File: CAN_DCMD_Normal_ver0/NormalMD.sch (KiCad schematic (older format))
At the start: 224 parts, among them P1 SWD, P10 OUT_1, P11 ENC_0, P13 ENC_1, P14 I/O_1, P15 OUT_0, P2 VALVE, P3 CAN, P4 CAN, P5 SERIAL, P6 I/O_0, P7 FAN, P8 BATT_IN, P9 BATT_IN, Q1 MOSFET_N, Q10 NPN, Q2 MOSFET_N, Q3 MOSFET_N, Q4 MOSFET_N, Q5 MOSFET_N, Q6 MOSFET_N, Q7 MOSFET_N, Q8 MOSFET_N, Q9 NPN, SW1 RST, SW3 SW0, SW4 SW1, U1 MAX3051, U11 POWER_ON, U12 SI8274, U14 SI8274, U15 AZ1086H, U16 LOGO, U17 AQM0802, U19 ADRESS, U2 BD9G101, U3 STM32F405RG, U4 SI8274, U5 SI8900, U6 ADC_~RST, U7 BD9G101G, U8 SI8274, U9 BD33FA1, Y1 8MHz

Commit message: 配置しただけで分かるやばいやつ
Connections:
- net VALVE0: now also U3.50 (TIM2_CH1_ETR/PA15)
- net VALVE1: now also U3.51 (PC10/UART4_TX/USART3_TX)
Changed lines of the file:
@@
 	1    0    0    -1
 $EndComp
+Text Label 4550 7125 2    50   ~ 0
+VALVE1
+Text Label 8950 5925 0    50   ~ 0
+VALVE0
 $EndSCHEMATC

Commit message: 電流制御MD(仮)配線(仮)完成(仮)
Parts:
- R37: value 50k -> 3.9k
- R38: value 10k -> 680
- R57, R60, R75, R76: value 2m -> 1m
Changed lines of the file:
@@
 P 5200 1800
 F 0 "R37" H 5270 1846 50  0000 L CNN
-F 1 "50k" H 5270 1755 50  0000 L CNN
+F 1 "3.9k" H 5270 1755 50  0000 L CNN
 F 2 "Resistor_SMD:R_0603_1608Metric" V 5130 1800 50  0001 C CNN
 F 3 "~" H 5200 1800 50  0001 C CNN
@@
 P 5200 2150
 F 0 "R38" H 5270 2196 50  0000 L CNN
-F 1 "10k" H 5270 2105 50  0000 L CNN
+F 1 "680" H 5270 2105 50  0000 L CNN
 F 2 "Resistor_SMD:R_0603_1608Metric" V 5130 2150 50  0001 C CNN
 F 3 "~" H 5200 2150 50  0001 C CNN
@@
 P 18650 6250
 F 0 "R57" V 18443 6250 50  0000 C CNN
-F 1 "2m" V 18534 6250 50  0000 C CNN
+F 1 "1m" V 18534 6250 50  0000 C CNN
 F 2 "Mizz_lib:R_2010_5025Metric" V 18580 6250 50  0001 C CNN
 F 3 "~" H 18650 6250 50  0001 C CNN
@@
 P 18650 6550
 F 0 "R60" V 18443 6550 50  0000 C CNN
-F 1 "2m" V 18534 6550 50  0000 C CNN
+F 1 "1m" V 18534 6550 50  0000 C CNN
 F 2 "Mizz_lib:R_2010_5025Metric" V 18580 6550 50  0001 C CNN
 F 3 "~" H 18650 6550 50  0001 C CNN
@@
 P 18650 9950
 F 0 "R75" V 18443 9950 50  0000 C CNN
-F 1 "2m" V 18534 9950 50  0000 C CNN
+F 1 "1m" V 18534 9950 50  0000 C CNN
 F 2 "Mizz_lib:R_2010_5025Metric" V 18580 9950 50  0001 C CNN
 F 3 "~" H 18650 9950 50  0001 C CNN
@@
 P 18650 10250
 F 0 "R76" V 18443 10250 50  0000 C CNN
-F 1 "2m" V 18534 10250 50  0000 C CNN
+F 1 "1m" V 18534 10250 50  0000 C CNN
 F 2 "Mizz_lib:R_2010_5025Metric" V 18580 10250 50  0001 C CNN
 F 3 "~" H 18650 10250 50  0001 C CNN

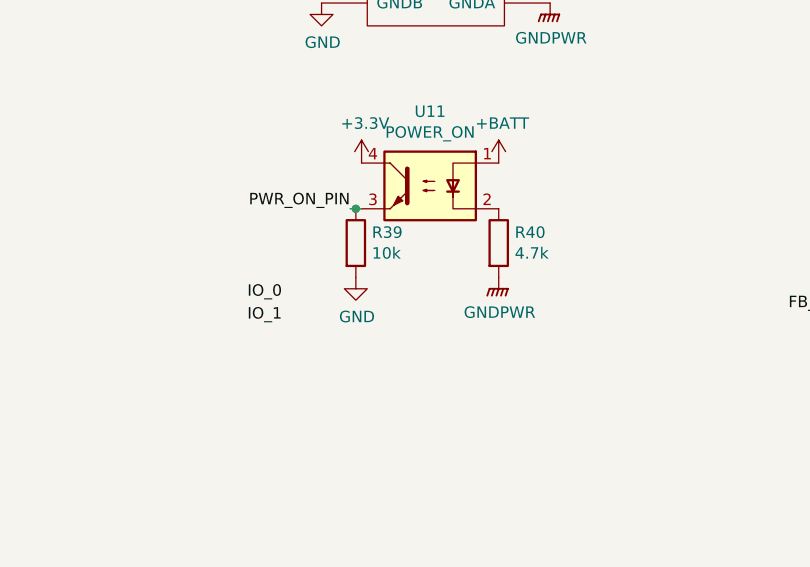
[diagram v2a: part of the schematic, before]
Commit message: 抵抗値を実装されているものに変更した
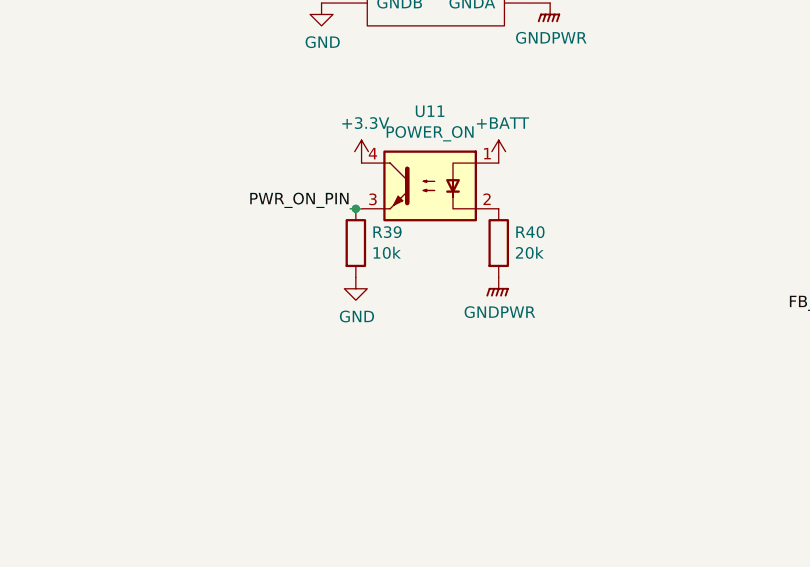
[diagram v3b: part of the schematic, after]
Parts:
- R40: value 4.7k -> 20k
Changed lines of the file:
@@
 EESchema Schematic File Version 4
-LIBS:NormalMD-cache
 EELAYER 30 0
 EELAYER END
@@
 Text Label 7800 13375 2    50   ~ 0
 USART2_RX
-Text Label 13950 4625 0    50   ~ 0
-IO_0
 $Comp
 L NormalMD-rescue:R-Device-MD_Enbarr_x2-rescue-F4_CAN_DCMD-rescue-SteerMD-rescue R4
@@
 P 15050 4375
 F 0 "R40" H 15120 4421 50  0000 L CNN
-F 1 "4.7k" H 15120 4330 50  0000 L CNN
+F 1 "20k" H 15120 4330 50  0000 L CNN
 F 2 "Resistor_SMD:R_0603_1608Metric" V 14980 4375 50  0001 C CNN
 F 3 "~" H 15050 4375 50  0001 C CNN
@@
 Text Label 8950 5225 0    50   ~ 0
 SW0
-Text Label 13950 4725 0    50   ~ 0
-IO_1
 Text Label 19200 2075 2    50   ~ 0
 OUT0_L

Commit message: 上げ忘れていた工大祭モータドライバ(前身開発基板)とJetsonNanoの電源基板関係
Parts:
- AMP1, AMP2: symbol Miz:TSC103 -> NormalMD-rescue:TSC103-Miz-NormalMD-rescue
- Q1, Q2, Q3, Q4, Q5, Q6, Q7, Q8: symbol NormalMD-rescue:MOSFET_N-Miz-F4_CAN_DCMD-rescue-SteerMD-rescue -> NormalMD-rescue:MOSFET_N-Miz-F4_CAN_DCMD-rescue-SteerMD-rescue-NormalMD-rescue
- U12, U14, U4, U8: symbol NormalMD-rescue:SI8274-Miz-F4_CAN_DCMD-rescue-SteerMD-rescue -> NormalMD-rescue:SI8274-Miz-F4_CAN_DCMD-rescue-SteerMD-rescue-NormalMD-rescue
- U16: symbol NormalMD-rescue:LOGO-myDevice-MD_Enbarr_x2-rescue-F4_CAN_DCMD-rescue-SteerMD-rescue -> NormalMD-rescue:LOGO-myDevice-MD_Enbarr_x2-rescue-F4_CAN_DCMD-rescue-SteerMD-rescue-NormalMD-rescue
- U2: symbol Miz:AP3211 -> NormalMD-rescue:AP3211-Miz
- U3: symbol NormalMD-rescue:STM32F405RG_excerpt-stm32f405rg_excerpt-Miz-MD_Enbarr_x2-rescue-F4_CAN_DCMD-rescue-SteerMD-rescue -> NormalMD-rescue:STM32F405RG_excerpt-stm32f405rg_excerpt-Miz-MD_Enbarr_x2-rescue-F4_CAN_DCMD-rescue-SteerMD-rescue-Norma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
- U5: symbol NormalMD-rescue:SI8900-Hori_lib-MD_Enbarr_x2-rescue-F4_CAN_DCMD-rescue-SteerMD-rescue -> NormalMD-rescue:SI8900-Hori_lib-MD_Enbarr_x2-rescue-F4_CAN_DCMD-rescue-SteerMD-rescue-NormalMD-rescue
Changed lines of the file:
@@
 EESchema Schematic File Version 4
+LIBS:NormalMD-cache
 EELAYER 30 0
 EELAYER END
@@
 $EndDescr
 $Comp
-L NormalMD-rescue:STM32F405RG_excerpt-stm32f405rg_excerpt-Miz-MD_Enbarr_x2-rescue-F4_CAN_DCMD-rescue-SteerMD-rescue U3
+L NormalMD-rescue:STM32F405RG_excerpt-stm32f405rg_excerpt-Miz-MD_Enbarr_x2-rescue-F4_CAN_DCMD-rescue-SteerMD-rescue-NormalMD-rescue U3
 U 1 1 5E0DD671
 P 6750 6025
@@
 $EndComp
 $Comp
-L NormalMD-rescue:SI8900-Hori_lib-MD_Enbarr_x2-rescue-F4_CAN_DCMD-rescue-SteerMD-rescue U5
+L NormalMD-rescue:SI8900-Hori_lib-MD_Enbarr_x2-rescue-F4_CAN_DCMD-rescue-SteerMD-rescue-NormalMD-rescue U5
 U 1 1 5E1CE2F1
 P 14775 2975
@@
 	18825 3000 18700 3000
 $Comp
-L Miz:AP3211 U2
+L NormalMD-rescue:AP3211-Miz U2
 U 1 1 5E588240
 P 4175 1850
@@
 Current0
 $Comp
-L NormalMD-rescue:LOGO-myDevice-MD_Enbarr_x2-rescue-F4_CAN_DCMD-rescue-SteerMD-rescue U16
+L NormalMD-rescue:LOGO-myDevice-MD_Enbarr_x2-rescue-F4_CAN_DCMD-rescue-SteerMD-rescue-NormalMD-rescue U16
 U 1 1 5D9F257F
 P 21750 2850
@@
 Connection ~ 10550 9875
 $Comp
-L Miz:LOGO_Monster #G1
+L NormalMD-rescue:LOGO_Monster-Miz #G1
 U 1 1 5E034095
 P 21725 2025
@@
 	18650 7650 18650 7725
 $Comp
-L Miz:TSC103 AMP2
+L NormalMD-rescue:TSC103-Miz-NormalMD-rescue AMP2
 U 1 1 5E2A539A
 P 18650 10875
@@
 	18100 12575 18650 12575
 $Comp
-L Miz:TSC103 AMP1
+L NormalMD-rescue:TSC103-Miz-NormalMD-rescue AMP1
 U 1 1 5E1F1A95
 P 18650 7175
@@
 $EndComp
 $Comp
-L NormalMD-rescue:SI8274-Miz-F4_CAN_DCMD-rescue-SteerMD-rescue U4
+L NormalMD-rescue:SI8274-Miz-F4_CAN_DCMD-rescue-SteerMD-rescue-NormalMD-rescue U4
 U 1 1 5DD10035
 P 16500 8325
@@
 $EndComp
 $Comp
-L NormalMD-rescue:MOSFET_N-Miz-F4_CAN_DCMD-rescue-SteerMD-rescue Q2
+L NormalMD-rescue:MOSFET_N-Miz-F4_CAN_DCMD-rescue-SteerMD-rescue-NormalMD-rescue Q2
 U 1 1 5DD192A7
 P 18000 8675
@@
 	17125 8825 17800 8825
 $Comp
-L NormalMD-rescue:MOSFET_N-Miz-F4_CAN_DCMD-rescue-SteerMD-rescue Q1
+L NormalMD-rescue:MOSFET_N-Miz-F4_CAN_DCMD-rescue-SteerMD-rescue-NormalMD-rescue Q1
 U 1 1 5DF47111
 P 18000 7925
@@
 	17650 7925 17800 7925
 $Comp
-L NormalMD-rescue:MOSFET_N-Miz-F4_CAN_DCMD-rescue-SteerMD-rescue Q5
+L NormalMD-rescue:MOSFET_N-Miz-F4_CAN_DCMD-rescue-SteerMD-rescue-NormalMD-rescue Q5
 U 1 1 5DF92975
 P 19300 7925
@@
 $EndComp
 $Comp
-L NormalMD-rescue:MOSFET_N-Miz-F4_CAN_DCMD-rescue-SteerMD-rescue Q6
+L NormalMD-rescue:MOSFET_N-Miz-F4_CAN_DCMD-rescue-SteerMD-rescue-NormalMD-rescue Q6
 U 1 1 5DF933DA
 P 19300 8675
@@
 Connection ~ 18100 8875
 $Comp
-L NormalMD-rescue:SI8274-Miz-F4_CAN_DCMD-rescue-SteerMD-rescue U12
+L NormalMD-rescue:SI8274-Miz-F4_CAN_DCMD-rescue-SteerMD-rescue-NormalMD-rescue U12
 U 1 1 5DFB7F6D
 P 20800 8325
@@
 $EndComp
 $Comp
-L NormalMD-rescue:SI8274-Miz-F4_CAN_DCMD-rescue-SteerMD-rescue U8
+L NormalMD-rescue:SI8274-Miz-F4_CAN_DCMD-rescue-SteerMD-rescue-NormalMD-rescue U8
 U 1 1 5E2F3D2B
 P 16500 12025
@@
 $EndComp
 $Comp
-L NormalMD-rescue:MOSFET_N-Miz-F4_CAN_DCMD-rescue-SteerMD-rescue Q4
+L NormalMD-rescue:MOSFET_N-Miz-F4_CAN_DCMD-rescue-SteerMD-rescue-NormalMD-rescue Q4
 U 1 1 5E2F3D35
 P 18000 12375
@@
 	17125 12525 17800 12525
 $Comp
-L NormalMD-rescue:MOSFET_N-Miz-F4_CAN_DCMD-rescue-SteerMD-rescue Q3
+L NormalMD-rescue:MOSFET_N-Miz-F4_CAN_DCMD-rescue-SteerMD-rescue-NormalMD-rescue Q3
 U 1 1 5E2F3D52
 P 18000 11625
@@
 	17650 11625 17800 11625
 $Comp
-L NormalMD-rescue:MOSFET_N-Miz-F4_CAN_DCMD-rescue-SteerMD-rescue Q7
+L NormalMD-rescue:MOSFET_N-Miz-F4_CAN_DCMD-rescue-SteerMD-rescue-NormalMD-rescue Q7
 U 1 1 5E2F3D61
 P 19300 11625
@@
 $EndComp
 $Comp
-L NormalMD-rescue:MOSFET_N-Miz-F4_CAN_DCMD-rescue-SteerMD-rescue Q8
+L NormalMD-rescue:MOSFET_N-Miz-F4_CAN_DCMD-rescue-SteerMD-rescue-NormalMD-rescue Q8
 U 1 1 5E2F3D6B
 P 19300 12375
@@
 Connection ~ 18100 12575
 $Comp
-L NormalMD-rescue:SI8274-Miz-F4_CAN_DCMD-rescue-SteerMD-rescue U14
+L NormalMD-rescue:SI8274-Miz-F4_CAN_DCMD-rescue-SteerMD-rescue-NormalMD-rescue U14
 U 1 1 5E2F3D79
 P 20800 12025
